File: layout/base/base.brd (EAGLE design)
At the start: 37.3 x 22.8 mm, 29 parts, among them IC2 FT232RL, IC3 74ACT125D, P1 FSM4JSMA-SMD, T1 BC848, T2 BC848

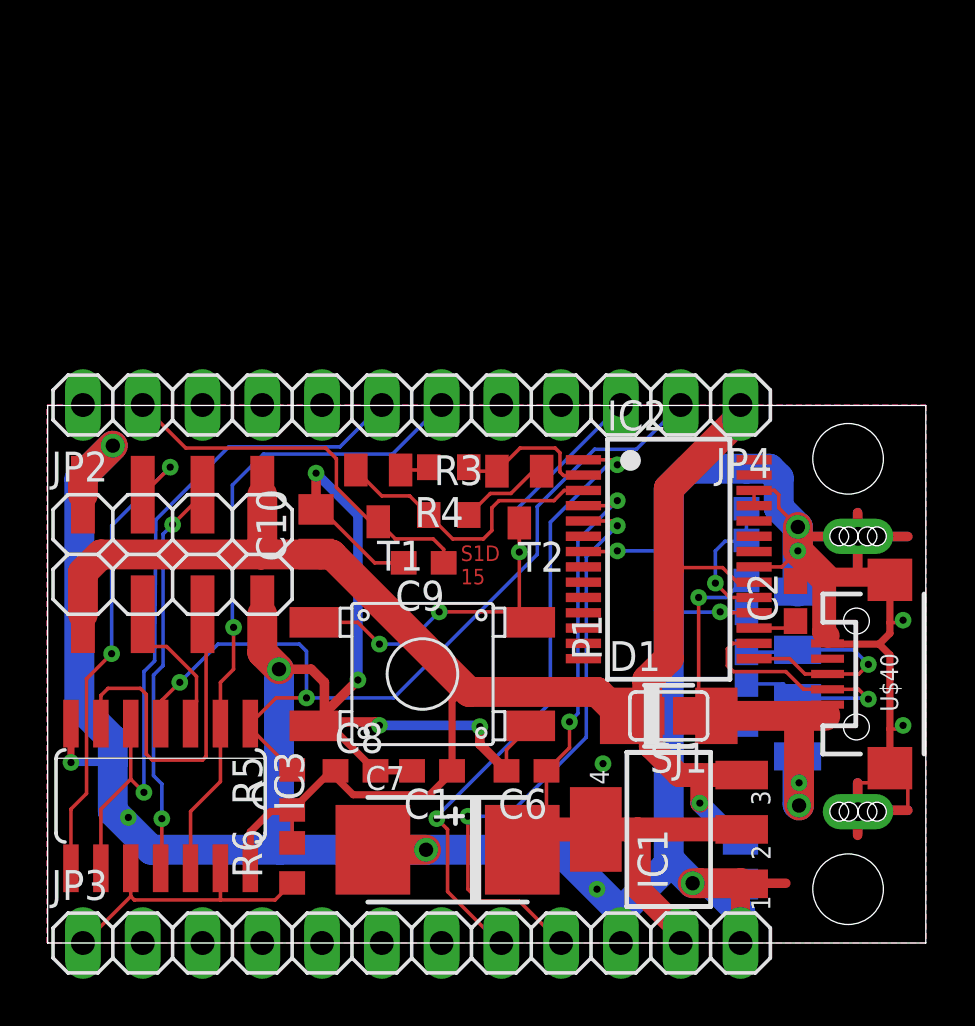
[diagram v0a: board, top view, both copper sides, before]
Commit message: base schematic w/o IC3 but w/ all dev board holes
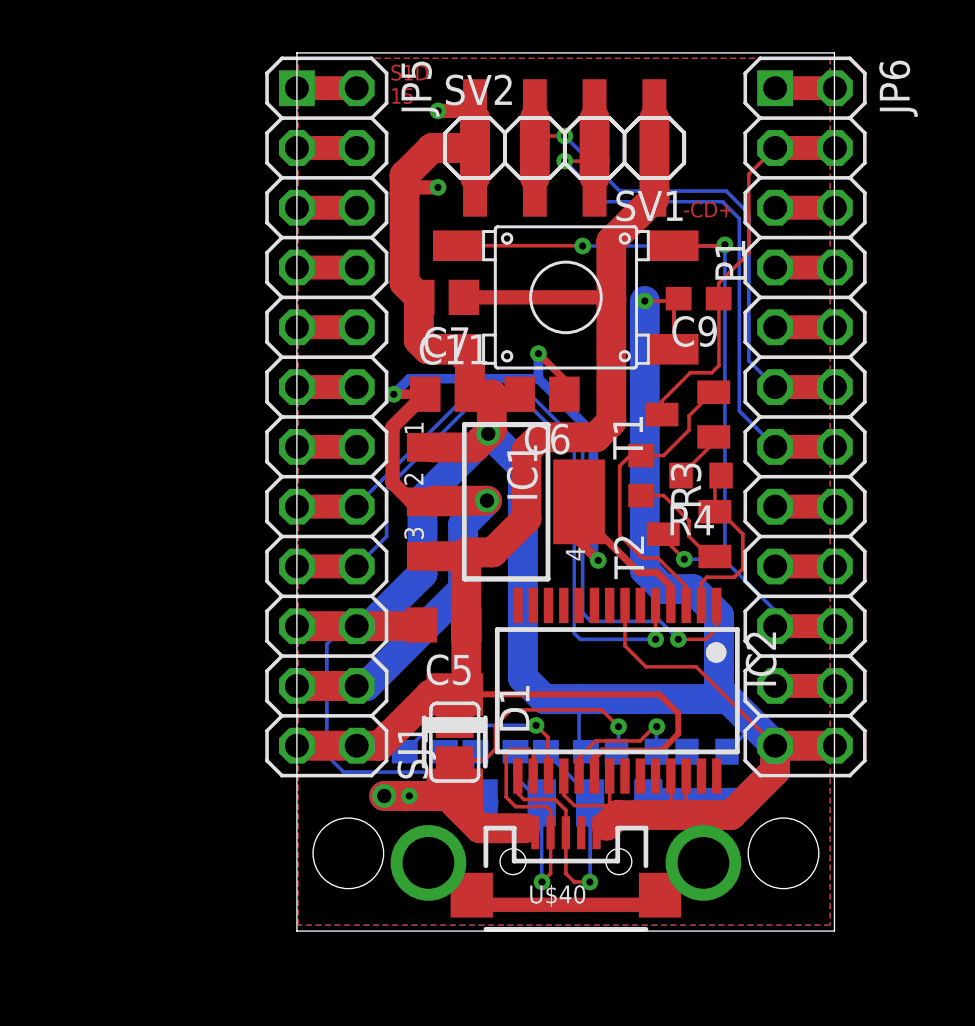
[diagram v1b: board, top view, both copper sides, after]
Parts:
- removed C1, C8: 100n, rcl:C0603
- removed C10: 22u, rcl-2:C0805
- removed IC3: 74ACT125D, 74xx-eu:SO14
- removed JP1: USBA-SMD-MALE, SparkFun-Connectors:USB-A-SMT-MALE
- removed JP2: (no value), pinhead-2:2X04SMD
- removed JP3, JP4: (no value), pinhead-2:1X12
- removed R5, R6: 10k, rcl-2:R0603
- added C11: 22u, rcl-2:C0805
- added JP5, JP6: (no value), pinhead-2:2X12
- added SV1, SV2: (no value), sid:1X4SMD-2.54
- added U$1: USB-MALE-SMT, sid:USB-MALE-SMT
- C6: value 100n -> 22u; device rcl:C0603 -> rcl-2:C0805
- C7: value 100u 6,3V -> 22u; device cap-master:7343-TE-D -> rcl-2:C0805
- moved C7 23.5 mm to (53.1, 61.5), turned to 180 degrees
- moved P1 17.1 mm to (58.4, 61.5)
- moved C2 17.0 mm to (52.4, 42.2), flipped to the bottom, turned to 180 degrees
- moved U$40 16.7 mm to (58.4, 36.1), turned to 0 degrees
- moved C9 16.2 mm to (64.0, 61.4)
- moved C5 16.1 mm to (53.2, 47.5), flipped to the top, turned to 180 degrees
- moved C6 16.0 mm to (57.4, 57.4)
- moved IC1 15.5 mm to (55.8, 52.8), turned to 270 degrees
- moved T1 13.6 mm to (63.6, 56.5), turned to 90 degrees
- moved R2 11.3 mm to (64.4, 42.2), turned to 0 degrees
- moved C3 10.9 mm to (55.4, 42.2), turned to 0 degrees
- moved R4 10.7 mm to (64.1, 53.9)
- moved R1 9.38 mm to (61.4, 42.2), turned to 0 degrees
- moved C4 9.20 mm to (58.4, 42.2), turned to 180 degrees
- moved D1 9.16 mm to (53.6, 42.6), turned to 270 degrees
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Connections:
- removed net N$10: IC3.11, JP2.6
- removed net N$35: IC3.3, JP2.3
- removed net N$36: IC3.6, JP2.5
- removed net N$9: IC3.8, JP2.4
- new net N$11: JP5.3, JP5.4
- new net N$13: JP5.5, JP5.6
- new net N$14: JP5.7, JP5.8
- new net N$15: JP5.10, JP5.9
- new net N$16: JP5.11, JP5.12
- new net N$17: JP5.13, JP5.14
- new net N$18: JP6.1, JP6.2
- new net N$19: JP6.5, JP6.6
- new net N$20: JP6.7, JP6.8
- new net N$21: JP6.10, JP6.9
- new net N$22: JP6.15, JP6.16
- new net N$23: JP6.17, JP6.18
- net +3V3: now also C11.1, JP5.21, JP5.22; no longer C7.+, JP3.11
- net +5V: now also C7.1, JP5.23, JP5.24, SV1.1, SV2.4; no longer C1.1, C10.1, C8.1, IC3.14, JP2.1, JP2.8, JP4.1, R5.1, R6.2
- net CI: now also JP6.11, JP6.12, SV1.3, SV2.2; no longer IC3.5, IC3.9, JP4.7
- net DI: now also JP6.13, JP6.14, SV1.2, SV2.3; no longer IC3.12, IC3.2, JP4.6
- net GND: now also C11.2, C7.2, JP5.19, JP5.20, JP6.23, JP6.24, SV1.4, SV2.1, U$1.GND1, U$1.S1, U$1.S2; no longer C1.2, C10.2, C7.-, C8.2, IC3.7, JP1.GND1, JP2.2, JP2.7, JP3.10, JP3.12
- net GPIO0: now also JP6.19, JP6.20; no longer JP4.3
- net N$2: now also U$1.VBUS1; no longer JP1.VBUS1
- net N$3: now also U$1.D+1; no longer JP1.D+1
- net N$4: now also U$1.D-1; no longer JP1.D-1
- net RST: now also JP6.3, JP6.4; no longer JP4.11
- net RX: now also JP5.15, JP5.16; no longer JP3.8
- net SSL: now also JP6.21, JP6.22; no longer IC3.1, IC3.4, JP4.2, R5.2
- net SSR: now also JP5.1, JP5.2; no longer IC3.10, IC3.13, JP3.1, R6.1
- net TX: now also JP5.17, JP5.18; no longer JP3.9
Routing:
- net GND: track 216.2 -> 165.9 mm, vias 18 -> 4
- net SSL: track 38.0 -> 2.54 mm, vias 2 -> 0
- net N$9: track 20.4 -> 0.00 mm, vias 2 -> 0
- net +3V3: track 32.1 -> 50.7 mm, vias 2 -> 4
- net +5V: track 78.9 -> 61.9 mm, vias 1 -> 0
- net N$10: track 16.9 -> 0.00 mm, vias 2 -> 0
- net N$36: track 14.7 -> 0.00 mm
- net GPIO0: track 22.1 -> 36.4 mm
- net SSR: track 12.6 -> 2.54 mm
- net CI: track 30.9 -> 23.4 mm
- net N$12: track 1.88 -> 8.41 mm, vias 0 -> 1
- net N$35: track 6.30 -> 0.00 mm
- net TX: track 25.5 -> 29.4 mm, vias 2 -> 1
- net N$2: track 20.0 -> 23.0 mm
- net RX: track 26.5 -> 29.4 mm, vias 2 -> 1
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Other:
- board size 37.3 x 22.8 mm -> 22.8 x 37.3 mm
- board text added: "-CD+"

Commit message: Bauteilbeschriftung der Platinen base und 4watt geordnet. Bestückungspläne hinzugefügt.
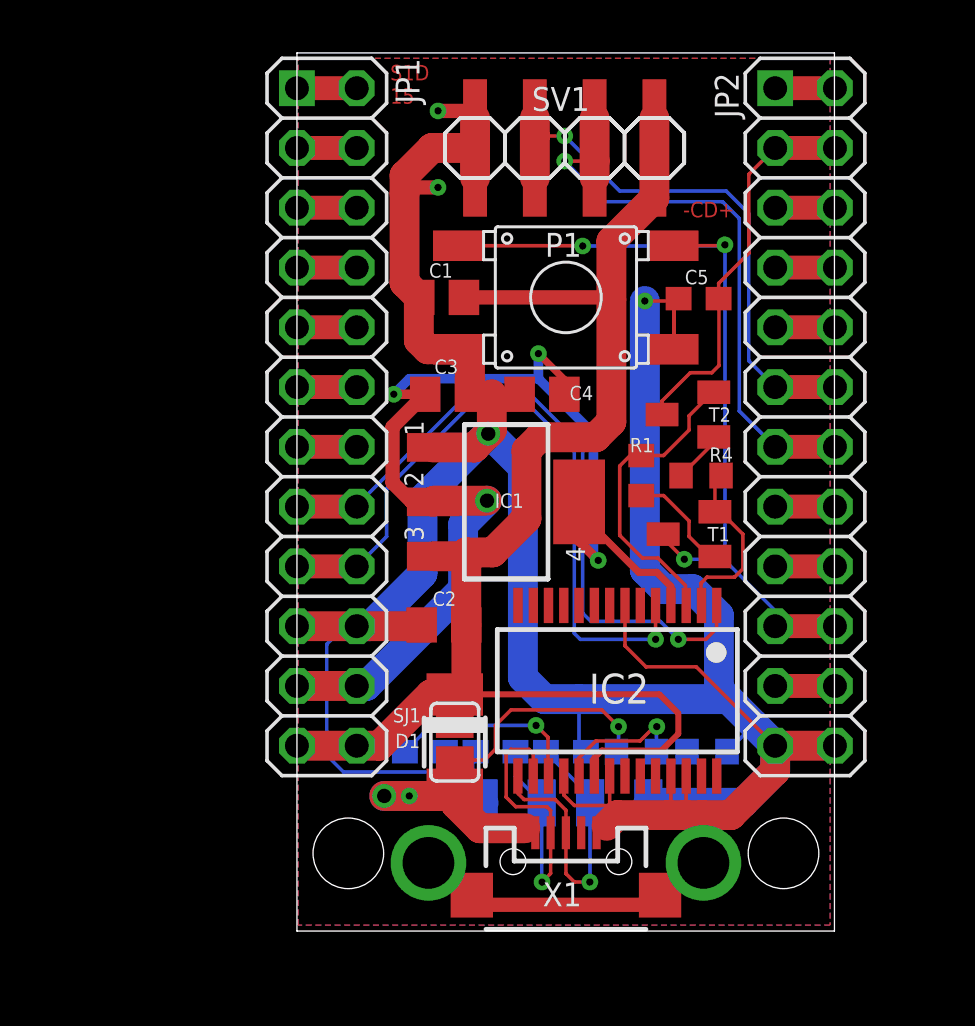
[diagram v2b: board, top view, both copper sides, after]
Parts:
- removed C11: 22u, rcl-2:C0805
- removed C9: 100n, rcl:C0603
- added C1: 22u, rcl-2:C0805
- added C8: 100n, rcl:C0603
- C2: value 100n -> 22u; device rcl:C0603 -> rcl-2:C0805
- C3, C4: value 22p -> 22u; device rcl:C0603 -> rcl-2:C0805
- C5: value 22u -> 100n; device rcl-2:C0805 -> rcl:C0603
- C6, C7: value 22u -> 22p; device rcl-2:C0805 -> rcl:C0603
- R1: value 4k7 -> 10k
- R2: value 10k -> 4k7
- moved C7 20.0 mm to (58.4, 42.2), flipped to the bottom
- moved C5 17.6 mm to (64.0, 61.4)
- moved C3 15.3 mm to (53.3, 57.4), flipped to the top
- moved C6 15.3 mm to (55.4, 42.2), flipped to the bottom, turned to 0 degrees
- moved C4 15.2 mm to (57.4, 57.4), flipped to the top
- moved R3 12.1 mm to (64.4, 42.2), flipped to the bottom, turned to 0 degrees
- moved R1 11.7 mm to (61.6, 53.9), flipped to the top, turned to 270 degrees
- moved C2 5.45 mm to (53.2, 47.5), flipped to the top
- moved T1 5.08 mm to (63.6, 51.4)
- moved T2 5.08 mm to (63.6, 56.5)
- moved R2 3.00 mm to (61.4, 42.2)
- renumbered JP5 to JP1, JP6 to JP2, U$1 to X2, U$40 to X1
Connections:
- net +3V3: now also C3.1, C4.1; no longer C11.1, C6.1
- net +5V: now also C1.1, C2.1; no longer C5.1, C7.1
- net GND: now also C1.2, C8.2, R3.1; no longer C11.2, C9.2, R2.1
- net GPIO0: now also T1.3; no longer T2.3
- net N$1: now also R1.1, T2.2; no longer R3.1, T1.2
- net N$12: now also C8.1; no longer C2.1
- net N$2: now also R2.2; no longer R1.2
- net N$3: now also C7.1; no longer C4.1
- net N$4: now also C6.1; no longer C3.1
- net N$5: now also T1.2; no longer T2.2
- net N$6: now also R2.1, R3.2; no longer R1.1, R2.2
- net N$7: now also R1.2, T1.1; no longer R3.2, T2.1
- net N$8: now also T2.1; no longer T1.1
- net RST: now also C5.1, T2.3; no longer C9.1, T1.3
